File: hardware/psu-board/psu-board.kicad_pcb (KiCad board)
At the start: 2 copper layers, 99.1 x 53.3 mm, 17 parts, among them J1 Motherboard connector, J2 Aux 1, J3 Sound To Light connector, J4 Aux 2, J5 Live In, J6 Neutral In, J7 Earth, U1 R-78E12-0.5, U2 R-78E5.0-0.5

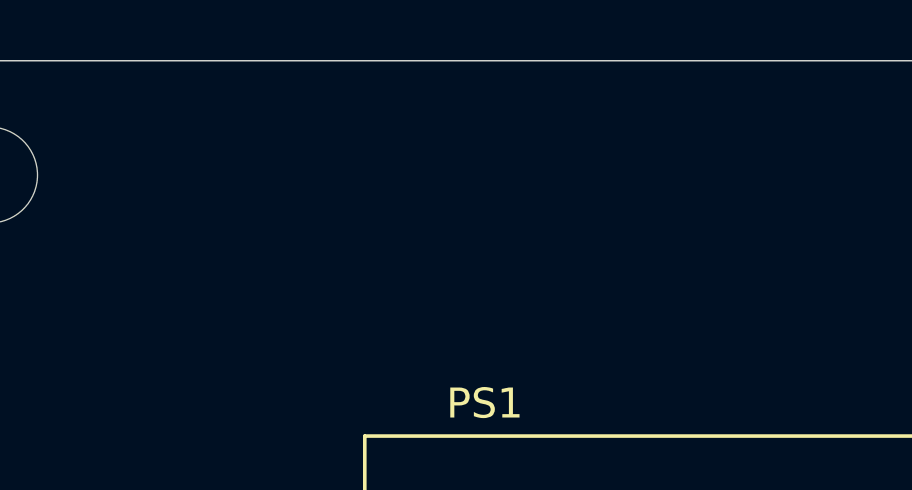
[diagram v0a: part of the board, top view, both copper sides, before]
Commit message: Sound to light board completed, PSU board completed
Rev As as ordered
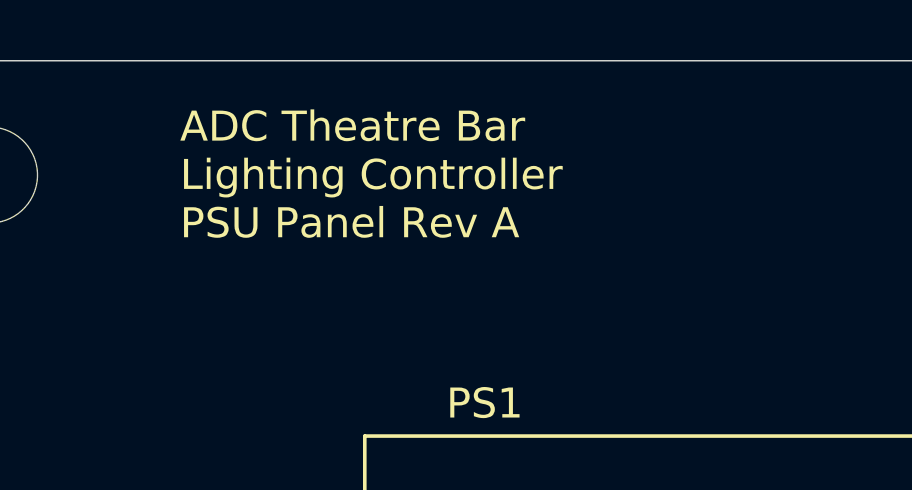
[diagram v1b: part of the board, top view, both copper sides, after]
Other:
- board text added: "ADC Theatre Bar Lighting Controller PSU Panel Rev A"
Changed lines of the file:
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@@
   (general
     (thickness 1.6)
-    (drawings 4)
+    (drawings 5)
     (tracks 34)
     (zones 0)
@@
   )
   (setup
-    (last_trace_width 1)
+    (last_trace_width 0.25)
     (user_trace_width 1)
     (user_trace_width 2)
@@
     (visible_elements FFFFFF7F)
     (pcbplotparams
-      (layerselection 0x010fc_ffffffff)
+      (layerselection 0x010f0_ffffffff)
       (usegerberextensions false)
       (usegerberattributes false)
@@
       (outputformat 1)
       (mirror false)
-      (drillshape 1)
+      (drillshape 0)
       (scaleselection 1)
-      (outputdirectory ""))
+      (outputdirectory "/Users/John/Desktop/psuboardgerber/"))
   )
   (net 0 "")
@@
     )
   )
+  (gr_text "ADC Theatre Bar\nLighting Controller\nPSU Panel Rev A" (at 104.14 64.77) (layer F.SilkS)
+    (effects (font (size 1 1) (thickness 0.15)) (justify left))
+  )
   (gr_line (start 93.98 114.3) (end 93.98 60.96) (layer Edge.Cuts) (width 0.05))
